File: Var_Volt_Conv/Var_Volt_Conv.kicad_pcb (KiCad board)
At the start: 6 copper layers, 114 x 120 mm, 98 parts, among them J101 Jack-DC, J102 Screw_Terminal_01x02, J103 Screw_Terminal_01x02, J201 Conn_01x05, Q101 AO3416, Q102 IRFML8244TRPBF, Q103 IRFML8244TRPBF, Q104 AO3407, Q105 AO3407, Q106 AO3407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

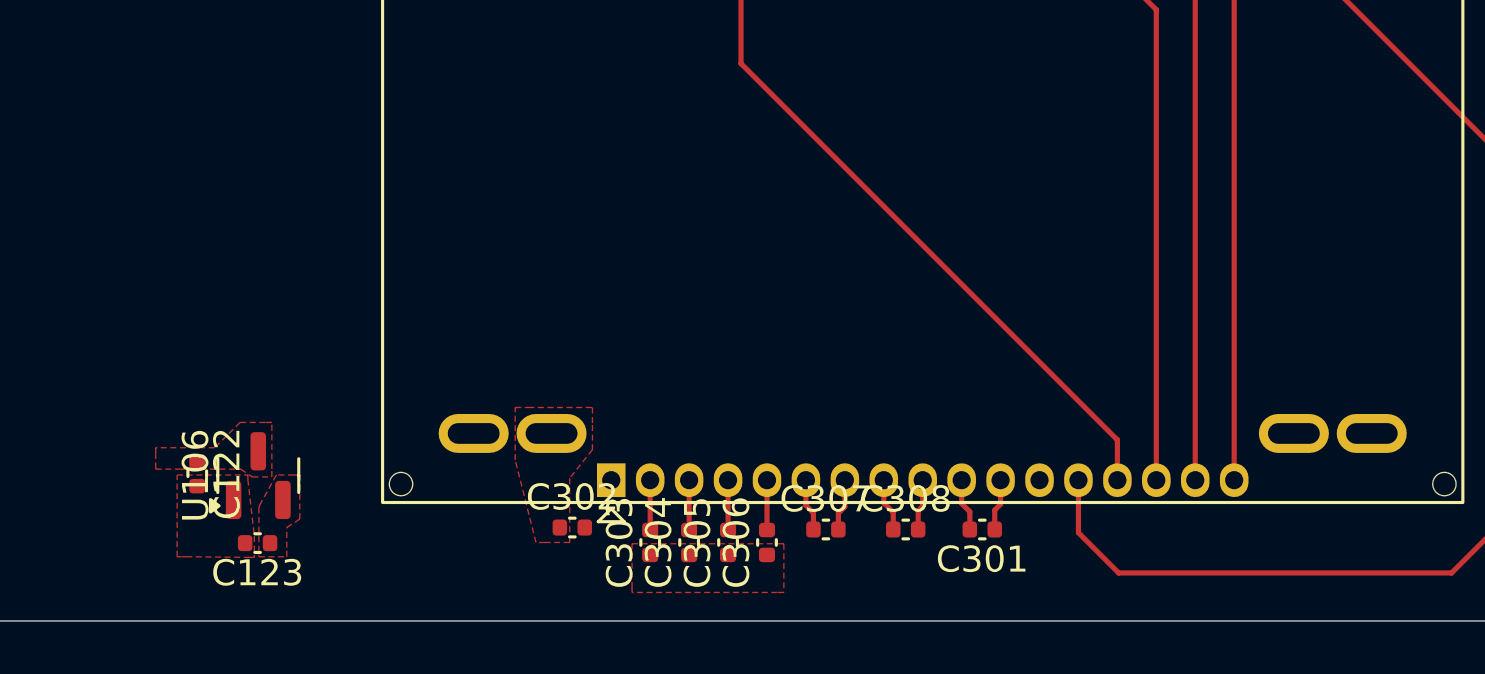
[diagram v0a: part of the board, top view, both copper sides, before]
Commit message: Corrected LCD screen footprint
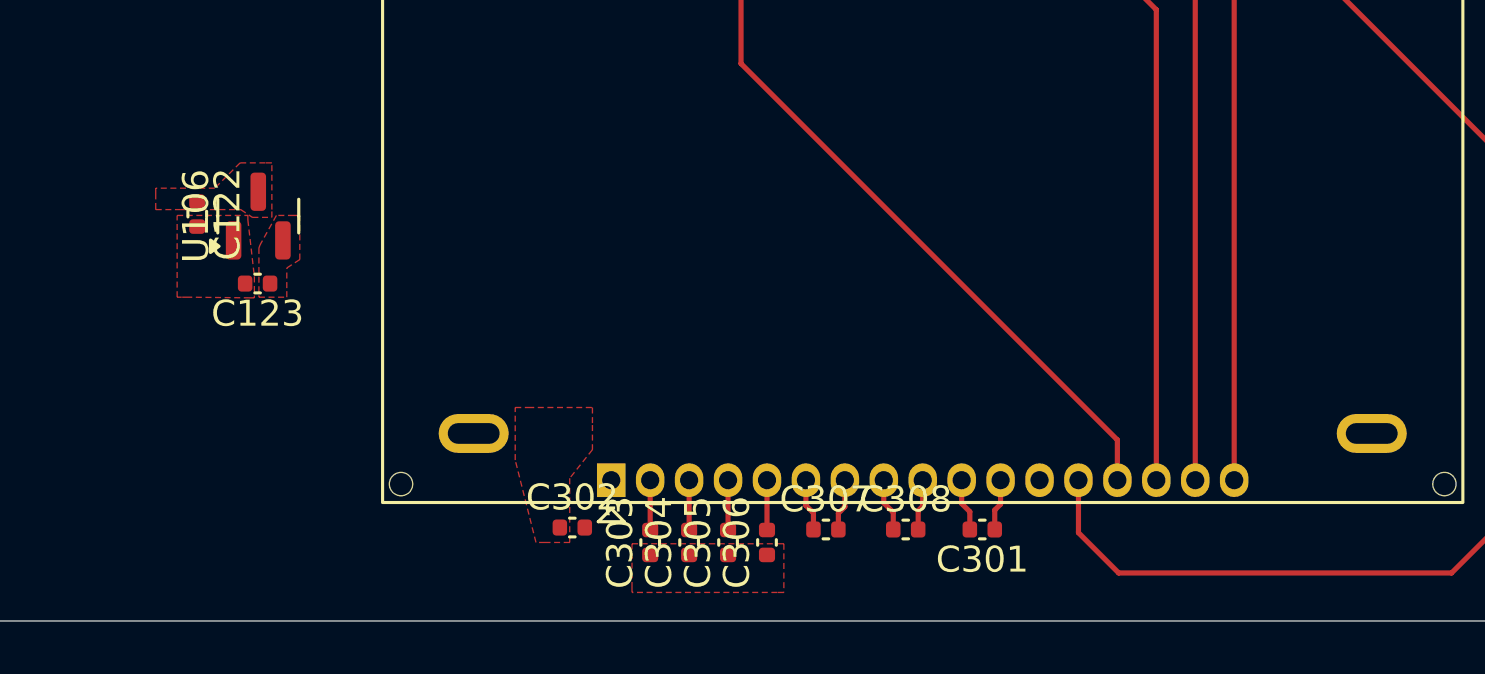
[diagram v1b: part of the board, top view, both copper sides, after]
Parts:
- moved C123 10.0 mm to (47.2, 127.0)
- moved U106 10.0 mm to (47.3, 124.4)
- moved C122 10.00 mm to (44.9, 124.3)
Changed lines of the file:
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@@
 		)
 		(pad "19" thru_hole oval
-			(at -2.3 -1.8)
+			(at 29.3 -1.8)
 			(size 2.7 1.5)
 			(drill oval 2 0.8)
@@
 			(pintype "power_in")
 		)
-		(pad "20" thru_hole oval
-			(at 26.3 -1.8)
-			(size 2.7 1.5)
-			(drill oval 2 0.8)
-			(layers "*.Cu" "*.Mask")
-			(remove_unused_layers no)
-		)
-		(pad "21" thru_hole oval
-			(at 29.3 -1.8)
-			(size 2.7 1.5)
-			(drill oval 2 0.8)
-			(layers "*.Cu" "*.Mask")
-			(remove_unused_layers no)
-		)
 		(model "${KIPRJMOD}/Project_Library/3d_Models/NHD-C12832A1Z.STEP"
 			(offset
@@
 	(footprint "Package_TO_SOT_SMD:SOT-23"
 		(layer "F.Cu")
-		(at 47.275 134.4 90)
+		(at 47.275 124.4 90)
 		(descr "SOT, 3 Pin (https://www.jedec.org/system/files/docs/to-236h.pdf variant AB), generated with kicad-footprint-generator ipc_gullwing_generator.py")
 		(tags "SOT TO_SOT_SMD")
@@
 	(footprint "Capacitor_SMD:C_0402_1005Metric"
 		(layer "F.Cu")
-		(at 47.25 137 180)
+		(at 47.25 127 180)
 		(descr "Capacitor SMD 0402 (1005 Metric), square (rectangular) end terminal, IPC_7351 nominal, (Body size source: IPC-SM-782 page 76, https://www.pcb-3d.com/wordpress/wp-content/uploads/ipc-sm-782a_amendment_1_and_2.pdf), generated with kicad-footprint-generator")
 		(tags "capacitor")
@@
 	(footprint "Capacitor_SMD:C_0402_1005Metric"
 		(layer "F.Cu")
-		(at 44.925 134.325 -90)
+		(at 44.925 124.325 -90)
 		(descr "Capacitor SMD 0402 (1005 Metric), square (rectangular) end terminal, IPC_7351 nominal, (Body size source: IPC-SM-782 page 76, https://www.pcb-3d.com/wordpress/wp-content/uploads/ipc-sm-782a_amendment_1_and_2.pdf), generated with kicad-footprint-generator")
 		(tags "capacitor")
@@
 		(polygon
 			(pts
-				(xy 44.15 134.375) (xy 46.875 134.375) (xy 46.875 134.55) (xy 47.125 136.725) (xy 47.125 137.55)
-				(xy 46.95 137.55) (xy 44.575 137.525) (xy 44.325 137.525) (xy 44.15 137.525) (xy 44.15 134.5)
+				(xy 44.15 124.375) (xy 46.875 124.375) (xy 46.875 124.55) (xy 47.125 126.725) (xy 47.125 127.55)
+				(xy 46.95 127.55) (xy 44.575 127.525) (xy 44.325 127.525) (xy 44.15 127.525) (xy 44.15 124.5)
 			)
 		)
@@
 		(polygon
 			(pts
-				(xy 46.6 134.15) (xy 47.05 134.45) (xy 47.8 134.45) (xy 47.8 134.15) (xy 47.8 132.35) (xy 47.55 132.35)
-				(xy 46.575 132.35) (xy 45.6 133.325) (xy 43.325 133.325) (xy 43.325 133.525) (xy 43.325 134.025)
-				(xy 43.325 134.15) (xy 44.3 134.15)
+				(xy 46.6 124.15) (xy 47.05 124.45) (xy 47.8 124.45) (xy 47.8 124.15) (xy 47.8 122.35) (xy 47.55 122.35)
+				(xy 46.575 122.35) (xy 45.6 123.325) (xy 43.325 123.325) (xy 43.325 123.525) (xy 43.325 124.025)
+				(xy 43.325 124.15) (xy 44.3 124.15)
 			)
 		)
@@
 		(polygon
 			(pts
-				(xy 47.3 137.525) (xy 48.375 137.525) (xy 48.375 137.175) (xy 48.375 136.4) (xy 48.875 136.075)
-				(xy 48.875 134.375) (xy 48.65 134.375) (xy 47.975 134.375) (xy 47.35 135.5) (xy 47.3 135.625) (xy 47.3 137.45)
+				(xy 47.3 127.525) (xy 48.375 127.525) (xy 48.375 127.175) (xy 48.375 126.4) (xy 48.875 126.075)
+				(xy 48.875 124.375) (xy 48.65 124.375) (xy 47.975 124.375) (xy 47.35 125.5) (xy 47.3 125.625) (xy 47.3 127.45)
 			)
 		)

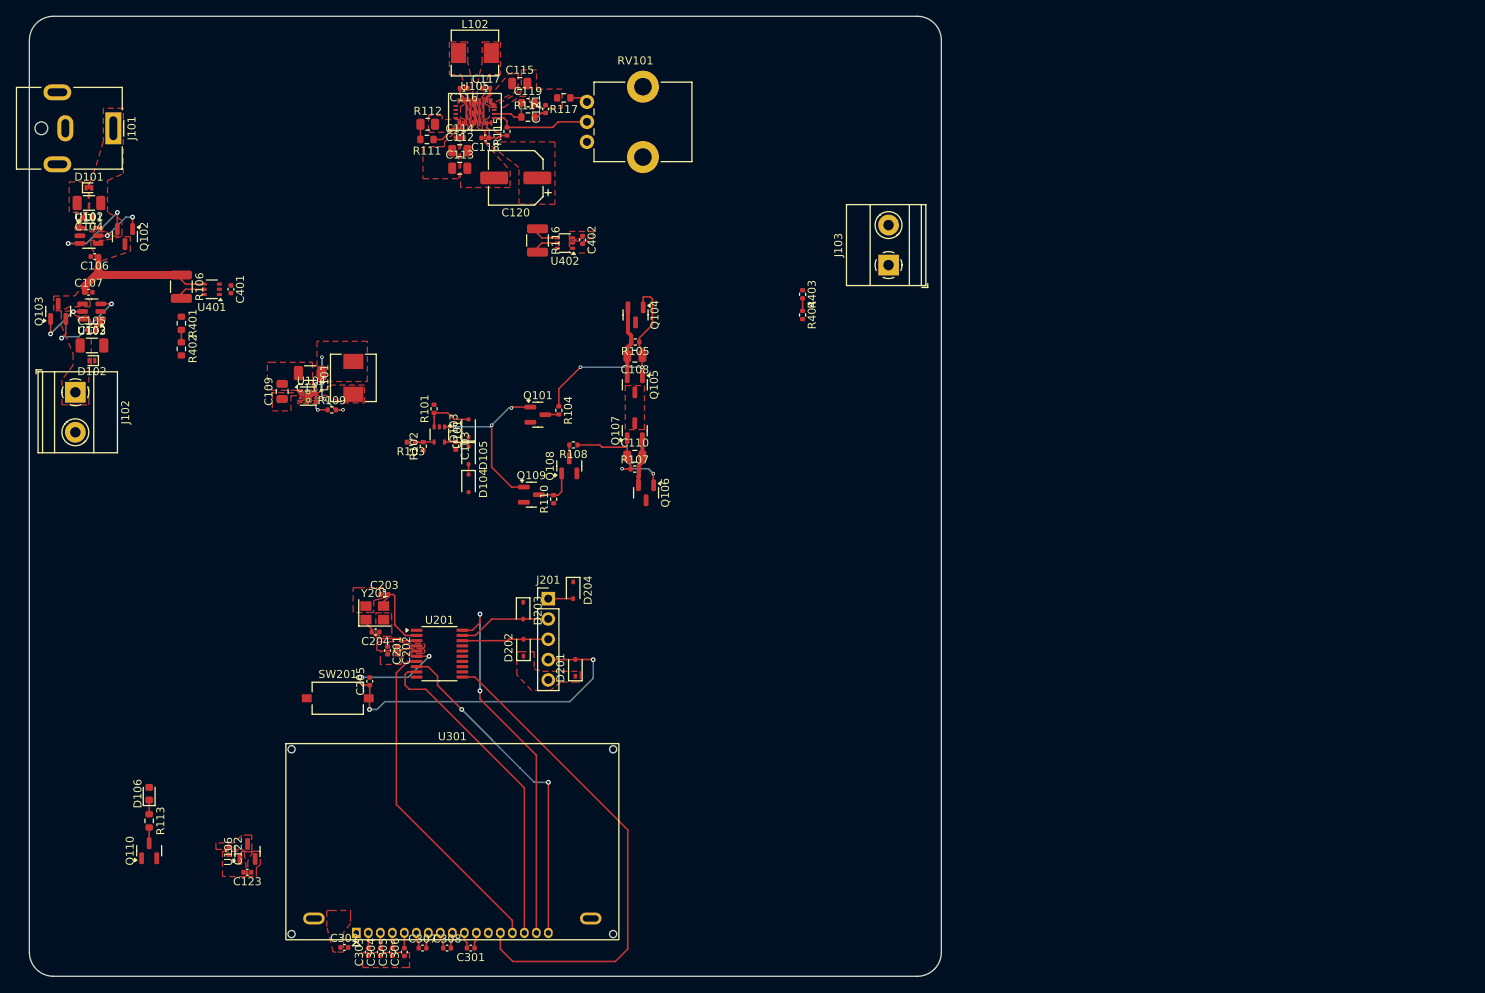
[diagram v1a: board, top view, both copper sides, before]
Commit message: Made reference designators for components invisible
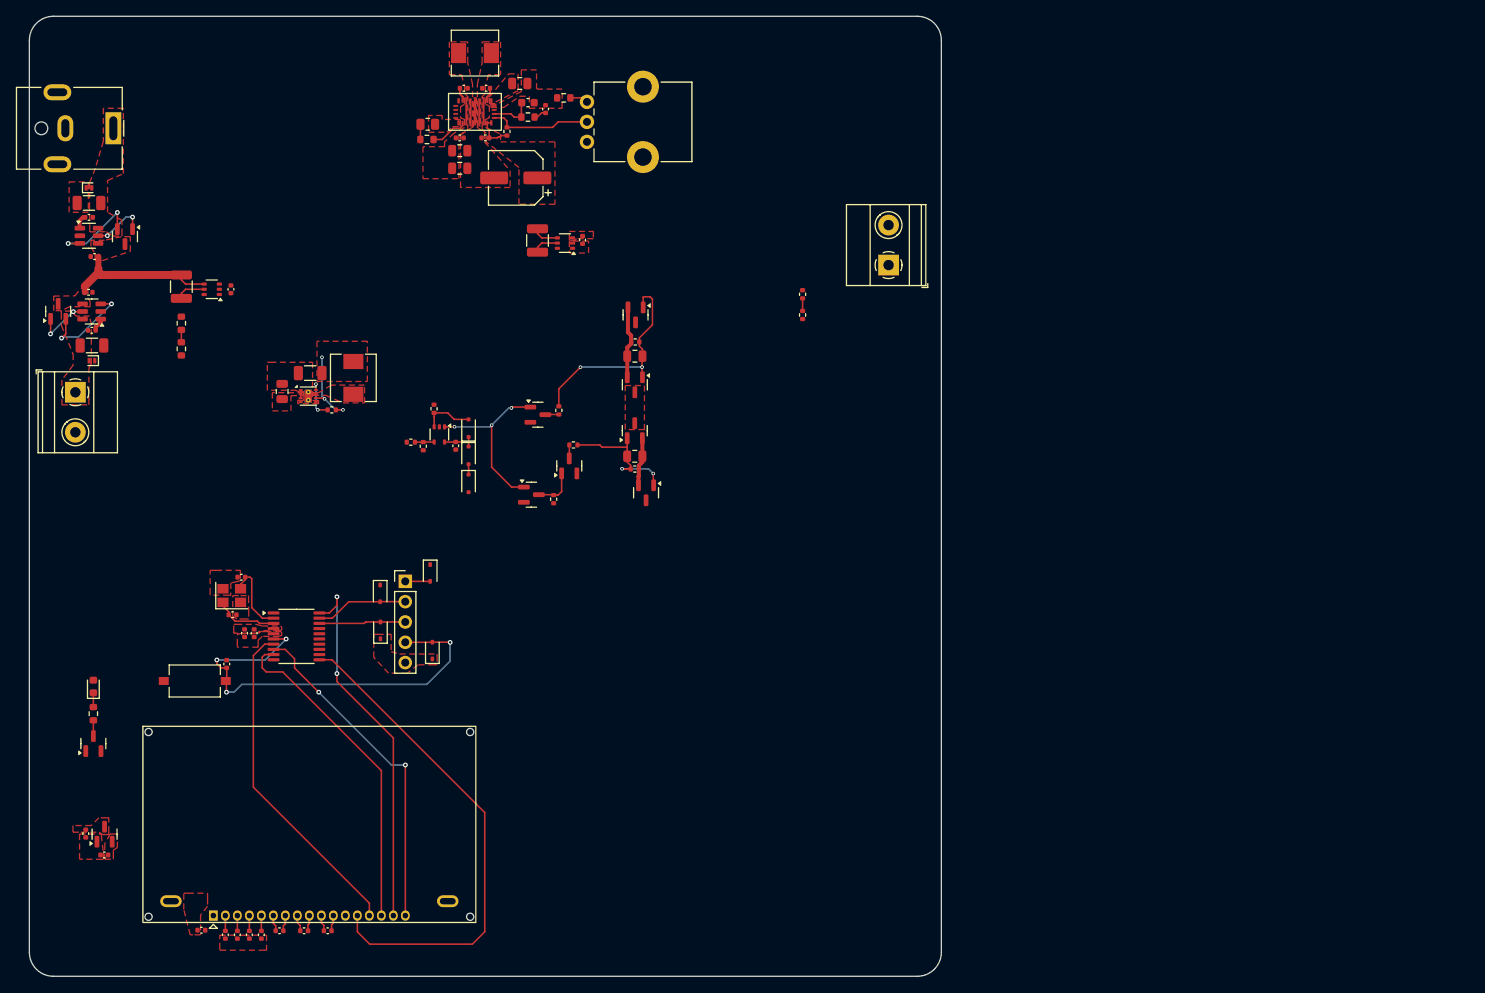
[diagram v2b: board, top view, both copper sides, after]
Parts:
- moved C201 18.0 mm to (46.9, 97.1)
- moved C203 18.0 mm to (46.5, 90.1)
- moved D201 18.0 mm to (70.4, 99.3)
- moved J201 18.0 mm to (67.0, 90.6)
- moved U106 18.0 mm to (29.4, 122.2)
- moved Y201 18.0 mm to (45.3, 92.4)
- moved C122 18.0 mm to (27.1, 122.2)
- moved C123 18.0 mm to (29.4, 124.8)
- moved C204 18.0 mm to (45.4, 94.8)
- moved C205 18.0 mm to (44.7, 101.0)
- moved C301 18.0 mm to (57.3, 134.3)
- moved C302 18.0 mm to (41.5, 134.2)
- moved C303 18.0 mm to (44.5, 134.8)
- moved C304 18.0 mm to (46.0, 134.8)
- moved C305 18.0 mm to (47.5, 134.8)
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
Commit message: Organized subsection layout on PCB
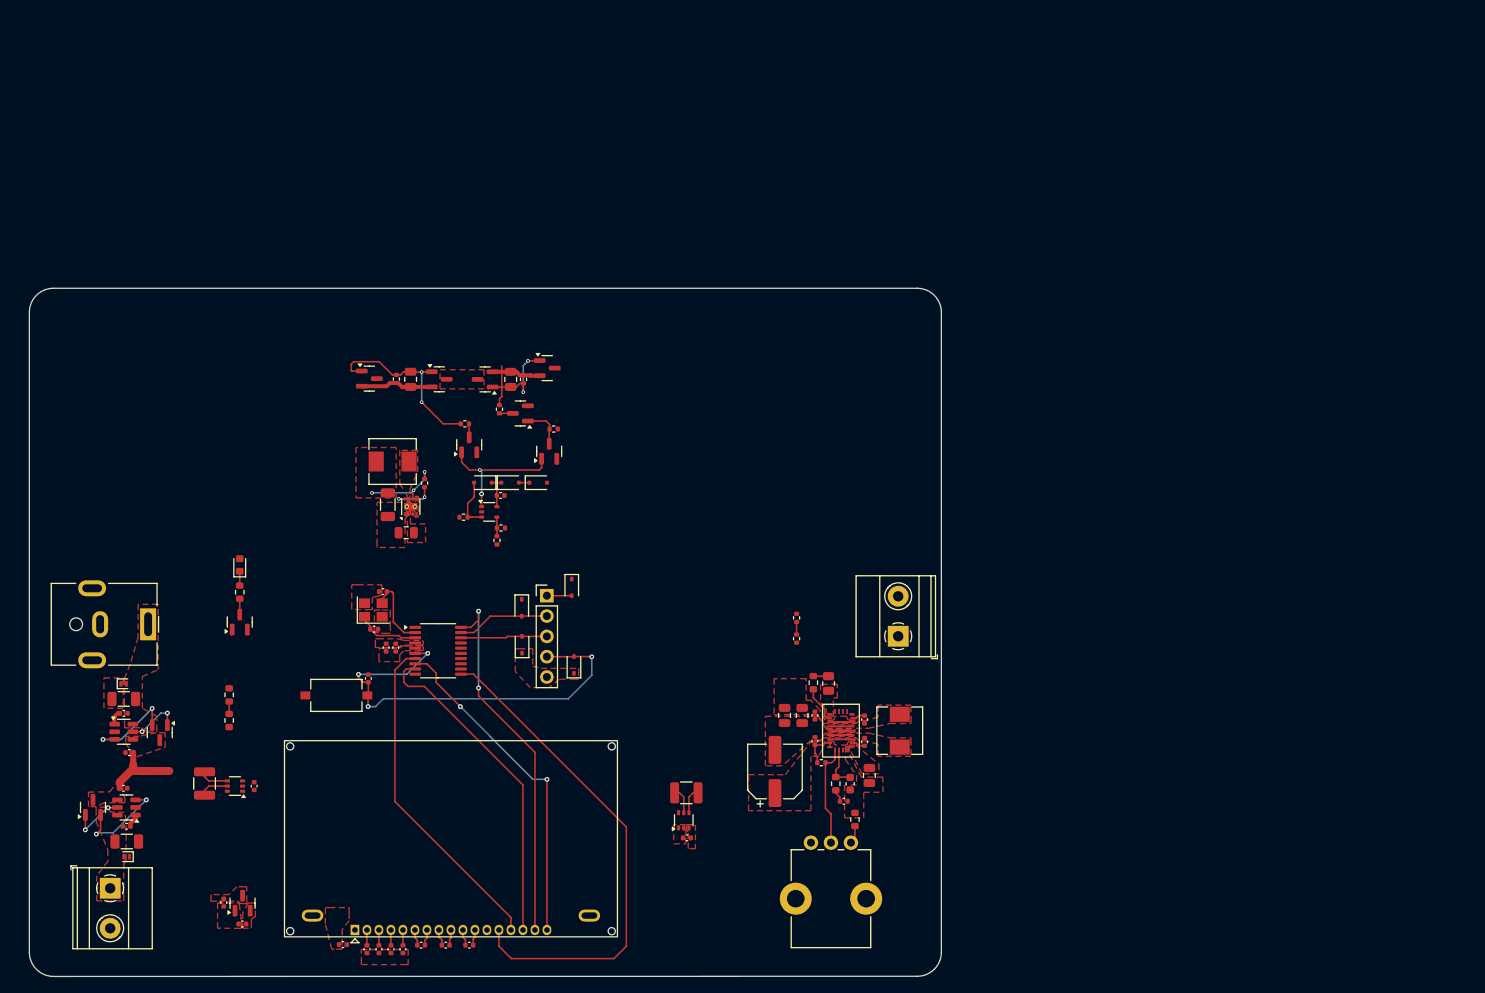
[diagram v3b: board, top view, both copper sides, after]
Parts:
- moved L102 100.0 mm to (128.8, 109.3), turned to -90 degrees
- moved R117 97.3 mm to (123.2, 120.4), turned to 90 degrees
- moved C115 96.9 mm to (125.0, 114.9), turned to -90 degrees
- moved C117 94.4 mm to (124.4, 110.7), turned to -90 degrees
- moved C121 94.2 mm to (121.8, 118.1), turned to 0 degrees
- moved C119 94.2 mm to (122.6, 115.9), turned to -90 degrees
- moved C116 93.5 mm to (124.4, 107.9), turned to 90 degrees
- moved RV101 92.0 mm to (117.7, 123.3), turned to -90 degrees
- moved R114 91.8 mm to (120.8, 115.9), turned to -90 degrees
- moved U105 89.9 mm to (121.5, 109.3), turned to -90 degrees
- moved R115 88.1 mm to (119.0, 113.3), turned to 0 degrees
- moved R112 86.0 mm to (119.9, 103.4), turned to -90 degrees
- moved C118 85.9 mm to (118.2, 110.6), turned to 90 degrees
- moved C114 84.8 mm to (118.2, 107.4), turned to -90 degrees
- moved R111 83.3 mm to (118.0, 103.3), turned to 90 degrees
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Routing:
- net SYSTEM_POWER_A: track 21.3 -> 15.5 mm
- net /[1] Power/COMP_OUT: track 22.1 -> 17.6 mm, vias 3 -> 2
- net /[1] Power/BUCK_PPM_GATE: track 26.9 -> 23.0 mm
- net /[1] Power/ST_PPM_GATE: track 17.1 -> 15.8 mm
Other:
- board size 114 x 120 mm -> 114 x 86 mm
- board text added: "3.3V Buck Converter"
- board text added: "3.3V Priority Multiplexer"
- board text added: "3V Power"
- board text added: "Buck-Boost Converter"
- board text added: "Input (I) Sensor"
- board text added: "Input (V) Sensor"
- board text added: "Input Power Orring"
- board text added: "Microcontroller Circuitry"
- board text added: "Output (I) Sensor"
- board text added: "Output (V) Sensor"
- board text added: "Power Ind."
